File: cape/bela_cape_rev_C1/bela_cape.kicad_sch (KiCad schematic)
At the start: 34 parts, among them J1 Conn_01x02, J10 Conn_01x04, J11 Conn_01x02, J2 Conn_01x04, J3 Conn_01x03, J4 Conn_01x03, J5 Conn_01x02, J6 Conn_01x02, J7 Conn_01x10, J8 Conn_01x10, J9 Conn_01x04, P1 BeagleBone_Black_Header

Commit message: First complete routing of C1 cape
(cherry picked from commit 8c5092941a0b3ec42f55098733fd0108b2086674)
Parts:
- J1: footprint Connector_Molex:Molex_KK-254_AE-6410-02A_1x02_P2.54mm_Vertical -> Connector_PinHeader_2.54mm:PinHeader_1x02_P2.54mm_Vertical
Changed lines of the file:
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@@
     (property "Reference" "J1" (id 0) (at 39.37 91.5502 0))
     (property "Value" "Conn_01x02" (id 1) (at 39.37 94.0871 0))
-    (property "Footprint" "Connector_Molex:Molex_KK-254_AE-6410-02A_1x02_P2.54mm_Vertical" (id 2) (at 39.37 99.06 0)
+    (property "Footprint" "Connector_PinHeader_2.54mm:PinHeader_1x02_P2.54mm_Vertical" (id 2) (at 39.37 99.06 0)
       (effects (font (size 1.27 1.27)) hide)
     )
@@
       (reference "#PWR024") (unit 1) (value "+5V") (footprint "")
     )
-    (path "/9e34013b-8051-4e0b-88b6-b650bff5b520/7cb84f83-78db-4799-8843-1a6b382f6114"
-      (reference "#PWR025") (unit 1) (value "GND") (footprint "")
-    )
-    (path "/9e34013b-8051-4e0b-88b6-b650bff5b520/29f4a8be-cd29-41b2-a9eb-1a13a996d4c1"
-      (reference "#PWR027") (unit 1) (value "GND") (footprint "")
-    )
-    (path "/9e34013b-8051-4e0b-88b6-b650bff5b520/800e6cb7-da14-417f-b31e-4bfa5763b429"
-      (reference "#PWR029") (unit 1) (value "GND") (footprint "")
-    )
-    (path "/9e34013b-8051-4e0b-88b6-b650bff5b520/6eee9127-72dd-4f7b-abc8-6ce3ac813d6c"
-      (reference "#PWR030") (unit 1) (value "GND") (footprint "")
-    )
     (path "/9062c558-1b23-4c83-8335-ef6d72e40b20"
       (reference "#PWR032") (unit 1) (value "+5V") (footprint "")
@@
     )
     (path "/c174e798-0d4a-4ee5-a279-22c30e2ae073/192408a6-4ca2-45dc-b931-ecb620d1338c"
-      (reference "#PWR?") (unit 1) (value "GNDA") (footprint "")
+      (reference "#PWR0169") (unit 1) (value "GNDA") (footprint "")
+    )
+    (path "/9e34013b-8051-4e0b-88b6-b650bff5b520/92ffdffc-7be5-4fe9-9b1d-41c919a3573d"
+      (reference "#PWR0170") (unit 1) (value "GNDA") (footprint "")
+    )
+    (path "/9e34013b-8051-4e0b-88b6-b650bff5b520/6c327b37-cc6c-4a96-985f-98d8e4059648"
+      (reference "#PWR0171") (unit 1) (value "GNDA") (footprint "")
+    )
+    (path "/9e34013b-8051-4e0b-88b6-b650bff5b520/2142d344-be19-4f00-bccf-06441ccc5e30"
+      (reference "#PWR0172") (unit 1) (value "GNDA") (footprint "")
+    )
+    (path "/9e34013b-8051-4e0b-88b6-b650bff5b520/01e05938-01fc-4fc6-8da7-f930903a2036"
+      (reference "#PWR0173") (unit 1) (value "GNDA") (footprint "")
+    )
+    (path "/9e34013b-8051-4e0b-88b6-b650bff5b520/707fb20c-600c-4c4b-b3c5-71e2ae96c45c"
+      (reference "#PWR0174") (unit 1) (value "GNDA") (footprint "")
     )
     (path "/2bd1dbb7-18bf-4e07-b6f1-ffaff520c436/112f7667-eada-4412-b923-6c968816a7c2"
@@
       (reference "C13") (unit 1) (value "47pF") (footprint "Capacitor_SMD:C_0603_1608Metric")
     )
-    (path "/9e34013b-8051-4e0b-88b6-b650bff5b520/62e631aa-9c44-43d4-afda-bec78217ed36"
-      (reference "C14") (unit 1) (value "0.1uF") (footprint "Capacitor_SMD:C_0603_1608Metric")
-    )
-    (path "/9e34013b-8051-4e0b-88b6-b650bff5b520/896bd42e-863b-472e-9925-e78d3d6da7f0"
+    (path "/9e34013b-8051-4e0b-88b6-b650bff5b520/936a4aa4-4870-498c-a7b0-4a589c03d3e3"
+      (reference "C14") (unit 1) (value "1uF") (footprint "Capacitor_SMD:C_0603_1608Metric")
+    )
+    (path "/9e34013b-8051-4e0b-88b6-b650bff5b520/30678166-213d-4389-a74f-de731b26b0bb"
       (reference "C15") (unit 1) (value "0.1uF") (footprint "Capacitor_SMD:C_0603_1608Metric")
     )
@@
       (reference "C16") (unit 1) (value "47uF") (footprint "Capacitor_SMD:C_1206_3216Metric")
     )
-    (path "/9e34013b-8051-4e0b-88b6-b650bff5b520/902fe62c-899e-49f8-abee-1b0d9dcc3f41"
-      (reference "C17") (unit 1) (value "47uF") (footprint "Capacitor_SMD:C_1206_3216Metric")
+    (path "/9e34013b-8051-4e0b-88b6-b650bff5b520/696a55ed-81bd-46fc-9032-ab1cd9fe0fd0"
+      (reference "C17") (unit 1) (value "0.1uF") (footprint "Capacitor_SMD:C_0603_1608Metric")
     )
     (path "/2bd1dbb7-18bf-4e07-b6f1-ffaff520c436/0ddc2aed-6ea9-42d4-80d5-c9f3a8740723"
@@
       (reference "C20") (unit 1) (value "0.1uF") (footprint "Capacitor_SMD:C_0603_1608Metric")
     )
-    (path "/9e34013b-8051-4e0b-88b6-b650bff5b520/700fce61-b7a3-4406-9bdc-fb5fa0c5ccbf"
-      (reference "C21") (unit 1) (value "0.1uF") (footprint "Capacitor_SMD:C_0603_1608Metric")
-    )
     (path "/ccc90cba-37a2-450c-9fab-b7472fcd4e10/b4f11c4c-8e94-41e0-9a70-fd538406bb6c"
       (reference "C22") (unit 1) (value "0.1uF") (footprint "Capacitor_SMD:C_0603_1608Metric")
@@
       (reference "IC3") (unit 1) (value "ES9080Q") (footprint "Bela:QFN40P500X500X80-41N-D")
     )
-    (path "/9e34013b-8051-4e0b-88b6-b650bff5b520/45a6ab05-575b-4cc8-b114-0bd91a3cbe56"
-      (reference "IC4") (unit 1) (value "LM4876") (footprint "bela_cape:SO8")
-    )
-    (path "/9e34013b-8051-4e0b-88b6-b650bff5b520/29214f98-782c-404e-bbdb-f46118625e79"
-      (reference "IC5") (unit 1) (value "LM4876") (footprint "bela_cape:SO8")
+    (path "/9e34013b-8051-4e0b-88b6-b650bff5b520/b78c5497-d416-401a-80a1-3a6376a4dcb1"
+      (reference "IC4") (unit 1) (value "PAM8406") (footprint "Package_SO:SO-16_3.9x9.9mm_P1.27mm")
     )
     (path "/ccc90cba-37a2-450c-9fab-b7472fcd4e10/b1b10d0e-e1dd-4657-ab48-32dc173842d1"
@@
     )
     (path "/ed642cee-c459-4943-85d1-c975f2cfa2b3"
-      (reference "J1") (unit 1) (value "Conn_01x02") (footprint "Connector_Molex:Molex_KK-254_AE-6410-02A_1x02_P2.54mm_Vertical")
+      (reference "J1") (unit 1) (value "Conn_01x02") (footprint "Connector_PinHeader_2.54mm:PinHeader_1x02_P2.54mm_Vertical")
     )
     (path "/eb1ce38c-caf1-4eac-9805-dab5da636f82"
@@
     )
     (path "/c174e798-0d4a-4ee5-a279-22c30e2ae073/ecbbc5b5-7507-435e-80f3-e5b72312658e"
-      (reference "J12") (unit 1) (value "Conn_01x03") (footprint "Connector_Molex:Molex_KK-254_AE-6410-03A_1x03_P2.54mm_Vertical")
+      (reference "J12") (unit 1) (value "Conn_01x03") (footprint "Connector_PinHeader_2.54mm:PinHeader_1x03_P2.54mm_Vertical")
     )
     (path "/c174e798-0d4a-4ee5-a279-22c30e2ae073/d41c4e43-b85b-482e-8143-06c1fa4f3d96"
-      (reference "J13") (unit 1) (value "Conn_01x03") (footprint "Connector_Molex:Molex_KK-254_AE-6410-03A_1x03_P2.54mm_Vertical")
+      (reference "J13") (unit 1) (value "Conn_01x03") (footprint "Connector_PinHeader_2.54mm:PinHeader_1x03_P2.54mm_Vertical")
     )
     (path "/c174e798-0d4a-4ee5-a279-22c30e2ae073/349a4925-f562-45ce-a147-e568ca325442"
-      (reference "J14") (unit 1) (value "Conn_01x03") (footprint "Connector_Molex:Molex_KK-254_AE-6410-03A_1x03_P2.54mm_Vertical")
+      (reference "J14") (unit 1) (value "Conn_01x03") (footprint "Connector_PinHeader_2.54mm:PinHeader_1x03_P2.54mm_Vertical")
     )
     (path "/c174e798-0d4a-4ee5-a279-22c30e2ae073/047ea503-e880-489d-812f-3d0035e438a2"
-      (reference "J15") (unit 1) (value "Conn_01x03") (footprint "Connector_Molex:Molex_KK-254_AE-6410-03A_1x03_P2.54mm_Vertical")
+      (reference "J15") (unit 1) (value "Conn_01x03") (footprint "Connector_PinHeader_2.54mm:PinHeader_1x03_P2.54mm_Vertical")
     )
     (path "/c174e798-0d4a-4ee5-a279-22c30e2ae073/9ca8070d-4161-4ba4-95e0-0a70f593f83e"
@@
     )
     (path "/ccc90cba-37a2-450c-9fab-b7472fcd4e10/50768e8d-6c06-4585-946d-337ae7200de6"
-      (reference "JP4") (unit 1) (value "SolderJumper_2_Bridged") (footprint "Jumper:SolderJumper-2_P1.3mm_Bridged_Pad1.0x1.5mm")
+      (reference "JP4") (unit 1) (value "SolderJumper_2_Bridged") (footprint "Bela:SolderJumper2_with_mask")
+    )
+    (path "/9e34013b-8051-4e0b-88b6-b650bff5b520/d2e39c82-1598-472a-892a-87140346e76a"
+      (reference "JP5") (unit 1) (value "SolderJumper_2_Bridged") (footprint "Jumper:SolderJumper-2_P1.3mm_Bridged_Pad1.0x1.5mm")
     )
     (path "/dd1db79d-77ca-4802-9ac0-4286dd4d6f0d"
@@
       (reference "R5") (unit 1) (value "220") (footprint "Resistor_SMD:R_0603_1608Metric")
     )
-    (path "/9e34013b-8051-4e0b-88b6-b650bff5b520/6e99eabc-e7fb-4b77-b28c-e78479953f5b"
-      (reference "R6") (unit 1) (value "22k") (footprint "Resistor_SMD:R_0603_1608Metric")
+    (path "/9e34013b-8051-4e0b-88b6-b650bff5b520/2cb6f24f-ffdd-422a-8c2e-ff8e66d0f563"
+      (reference "R6") (unit 1) (value "100k") (footprint "Resistor_SMD:R_0603_1608Metric")
     )
     (path "/9e34013b-8051-4e0b-88b6-b650bff5b520/4515842f-6ea2-41d9-831f-0d62c09f62fd"
@@
       (reference "R8") (unit 1) (value "22k") (footprint "Resistor_SMD:R_0603_1608Metric")
     )
-    (path "/9e34013b-8051-4e0b-88b6-b650bff5b520/fa2c55f7-1a44-4e67-ba7b-c970ac448aab"
-      (reference "R9") (unit 1) (value "43k") (footprint "Resistor_SMD:R_0603_1608Metric")
-    )
-    (path "/9e34013b-8051-4e0b-88b6-b650bff5b520/102fb582-789d-41f3-8d40-40394bed5fbe"
-      (reference "R10") (unit 1) (value "43k") (footprint "Resistor_SMD:R_0603_1608Metric")
+    (path "/9e34013b-8051-4e0b-88b6-b650bff5b520/54328fb4-29b1-4bda-8020-019de83cd549"
+      (reference "R9") (unit 1) (value "100k") (footprint "Resistor_SMD:R_0603_1608Metric")
     )
     (path "/bb36e87c-1293-4085-a75f-6f20a7c42ef4"

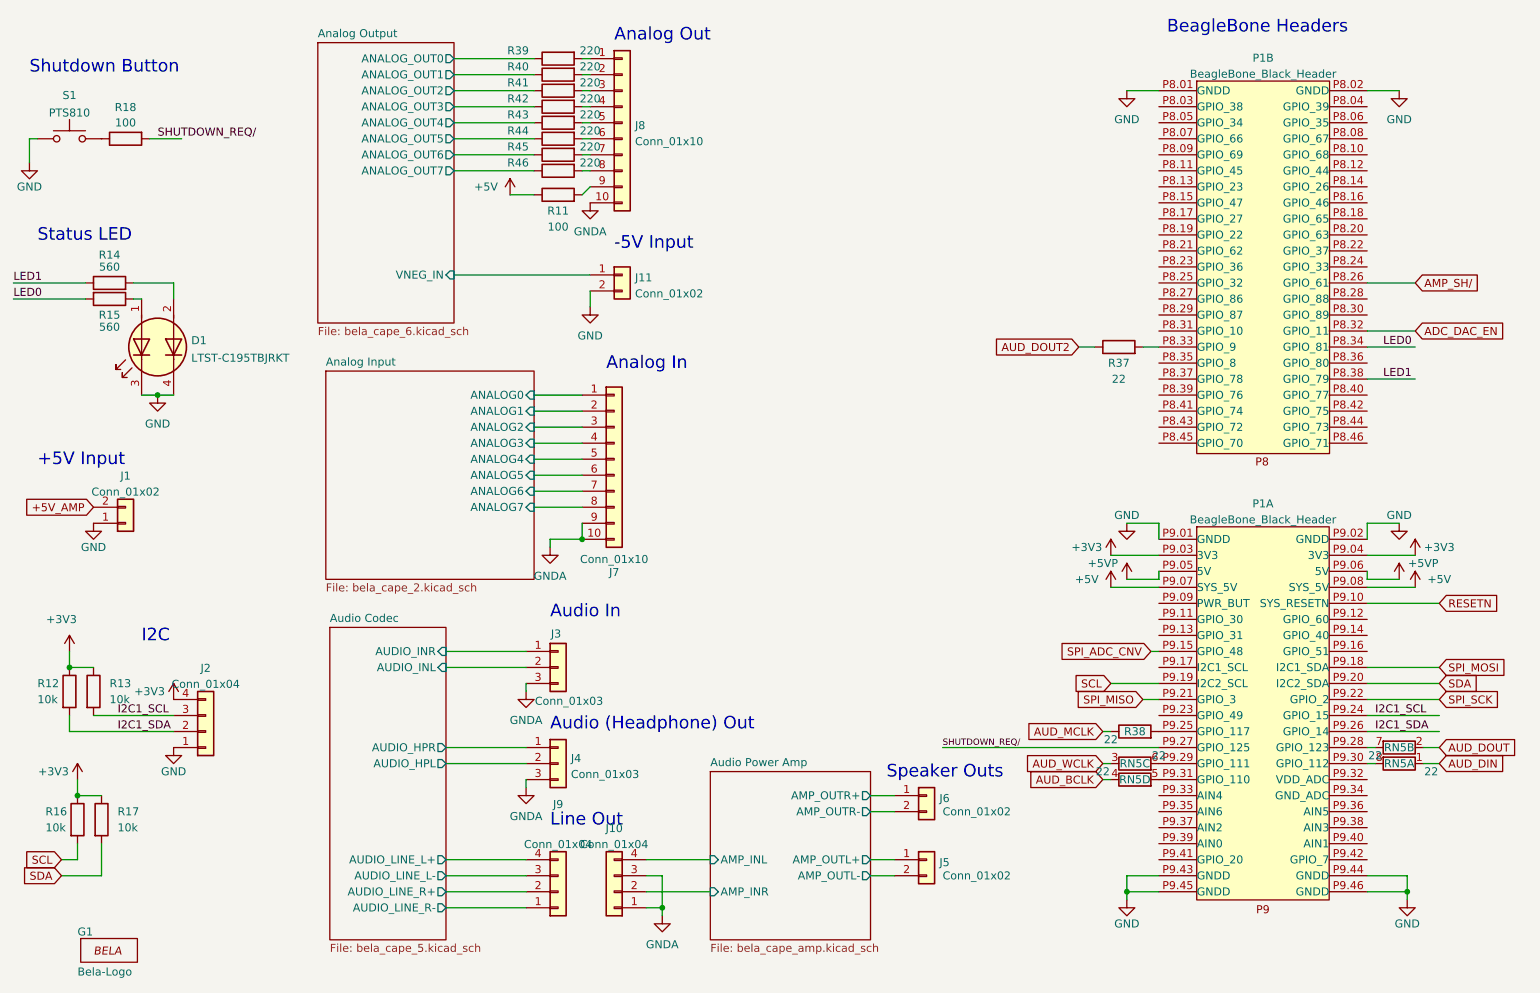
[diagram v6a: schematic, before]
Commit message: Bela cape C1: renumber components
(cherry picked from commit 6ebfe9c44bb7559ffb4c9dbd092e49803523e6a1)
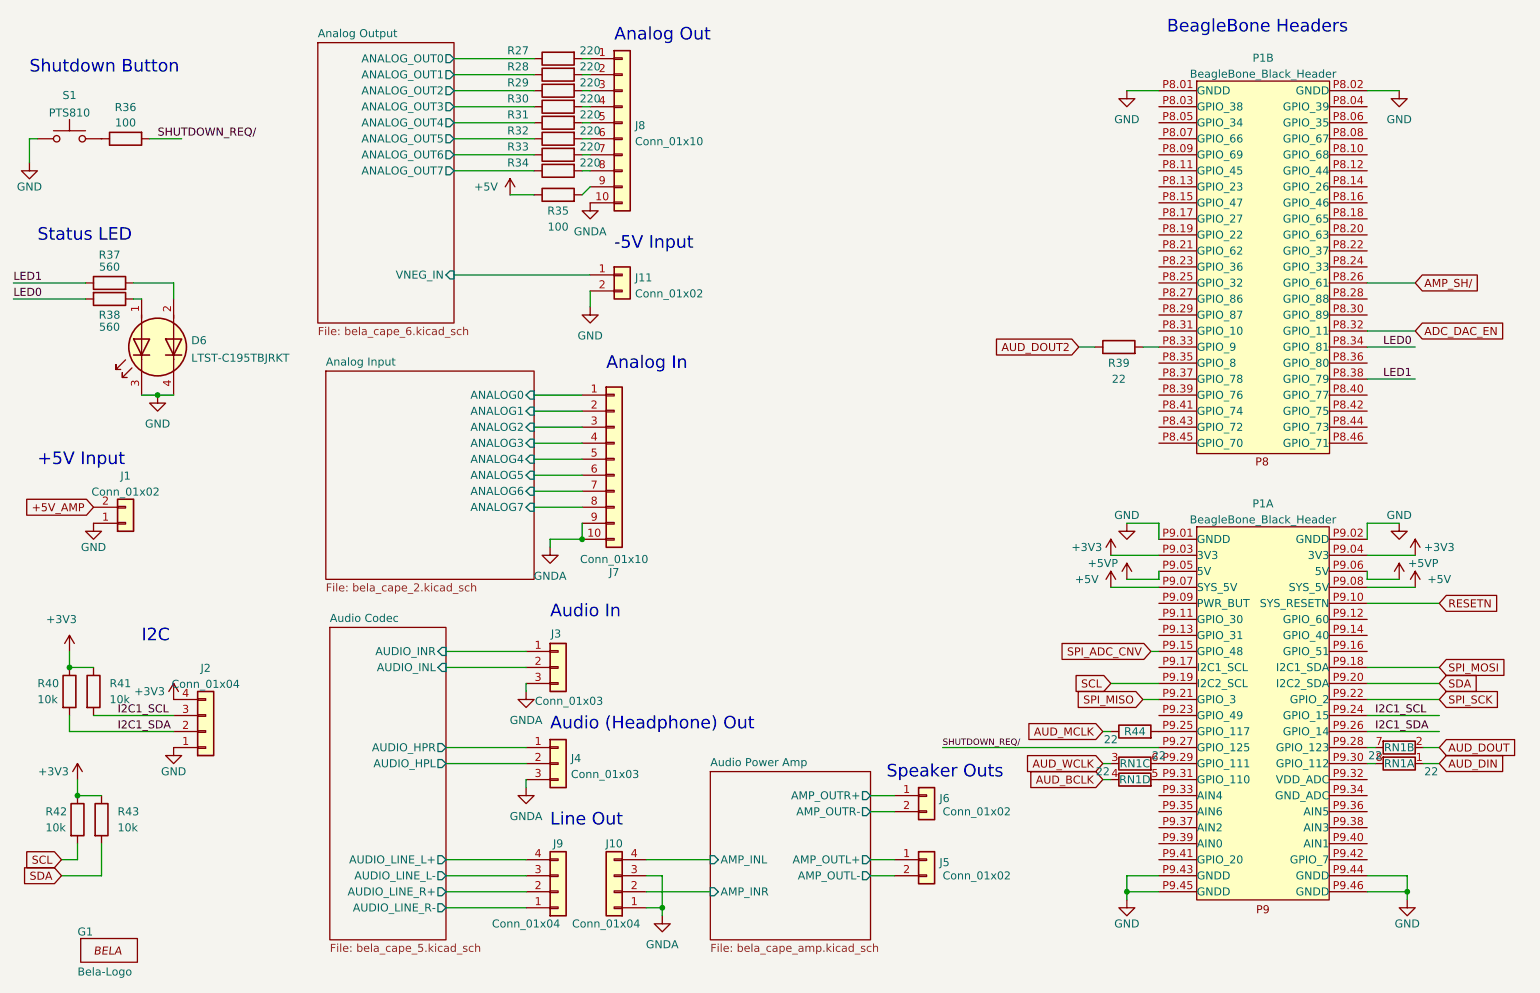
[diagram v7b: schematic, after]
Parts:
- renumbered D1 to D6, R39 to R27, R40 to R28, R41 to R29, R42 to R30, R43 to R31, R44 to R32, R45 to R33, R46 to R34, R11 to R35, R18 to R36, R14 to R37, R15 to R38, R37 to R39, R12 to R40, R13 to R41, R16 to R42, R17 to R43, R38 to R44, RN5 to RN1
